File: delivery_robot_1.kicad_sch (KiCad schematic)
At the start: 27 parts, among them J1 SWD, J2 XT30PW-M, J4 BOOT0 jumper, SW1 RESET, U1 STM32F091RCTx, Y3 8MHz

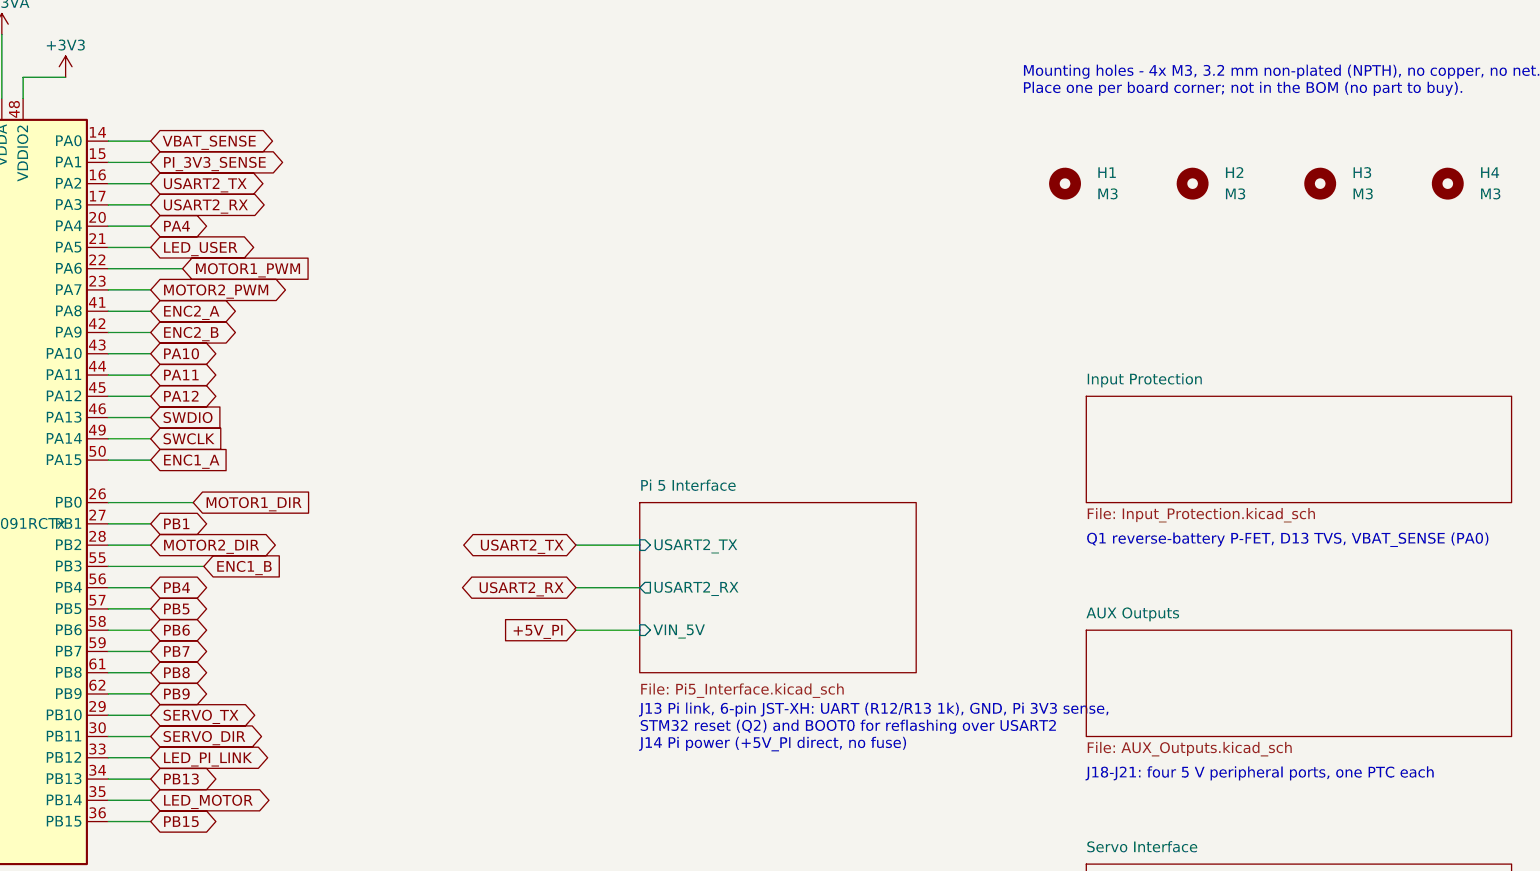
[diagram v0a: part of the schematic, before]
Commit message: Switch AUX ports to top-entry JST XH; drop encoder pull-ups and Pi sense
- J18-J21 (peripheral 5 V ports) are now top-entry JST XH B2B-XH-A:
  cables plug in from above, which suits a flat board you reach into,
  and the footprint drops from 107 to 58 mm2 per port. Use pre-made
  2-pin XH cables, so no crimping.
- Remove the DNP encoder pull-ups R48-R51. If the am-3651 outputs turn
  out to be open-collector, bodge 4.7k from each A/B line to ENCn_5V
  (noted on the Motor Control sheet).
- Remove the Pi-alive sense R44/R45. PA1 is a spare pin again (J8 pin
  2); the Pi's 3V3 on J13 still enables the AUX buck through D15.
- Board: same edits as Update PCB from Schematic (J18-J21 swapped,
  six resistors deleted, PA1 net restored on U1/J8); the parked parts
  are re-grouped beside the board. Venya's tracks unchanged (87).
- Docs, README and schematic PDF updated.

ERC 0/0. DRC: 0 errors, 3 existing text-size warnings, parity clean.
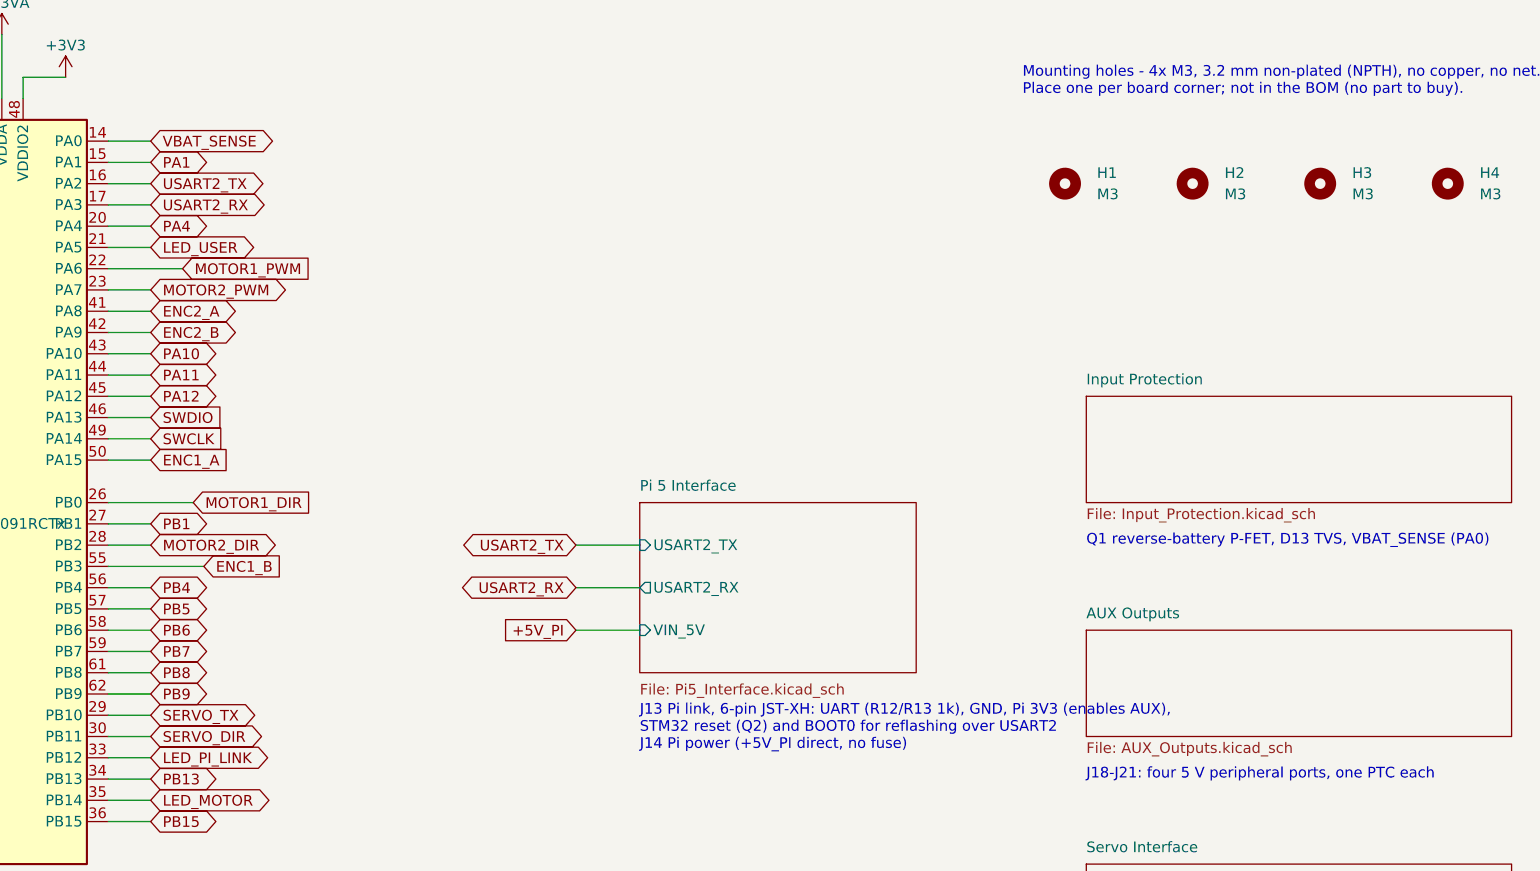
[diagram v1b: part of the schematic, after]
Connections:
- net PI_3V3_SENSE renamed PA1
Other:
- note added: "J13 Pi link, 6-pin JST-XH: UART (R12/R13 1k), GND, Pi 3V3 (enables AUX), STM32 reset (Q2) and BOOT0 for reflashing over USART2 J14 Pi power (+5V_PI direct, no fuse)"
- note removed: "J13 Pi link, 6-pin JST-XH: UART (R12/R13 1k), GND, Pi 3V3 sense, STM32 reset (Q2) and BOOT0 for reflashing over USART2 J14 Pi power (+5V_PI direct, no fuse)"
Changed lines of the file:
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@@
 		)
 	)
-	(text "J13 Pi link, 6-pin JST-XH: UART (R12/R13 1k), GND, Pi 3V3 sense,\nSTM32 reset (Q2) and BOOT0 for reflashing over USART2\nJ14 Pi power (+5V_PI direct, no fuse)"
+	(text "J13 Pi link, 6-pin JST-XH: UART (R12/R13 1k), GND, Pi 3V3 (enables AUX),\nSTM32 reset (Q2) and BOOT0 for reflashing over USART2\nJ14 Pi power (+5V_PI direct, no fuse)"
 		(exclude_from_sim no)
 		(at 276.86 189.23 0)
@@
 		)
 	)
-	(global_label "PI_3V3_SENSE"
+	(global_label "PA1"
 		(shape bidirectional)
 		(at 218.44 124.46 0)
